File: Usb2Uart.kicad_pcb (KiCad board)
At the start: 2 copper layers, 46.2 x 16.2 mm, 46 parts, among them Q1 DVIUC6-4SC6, U1 DLW21SN900SQ2

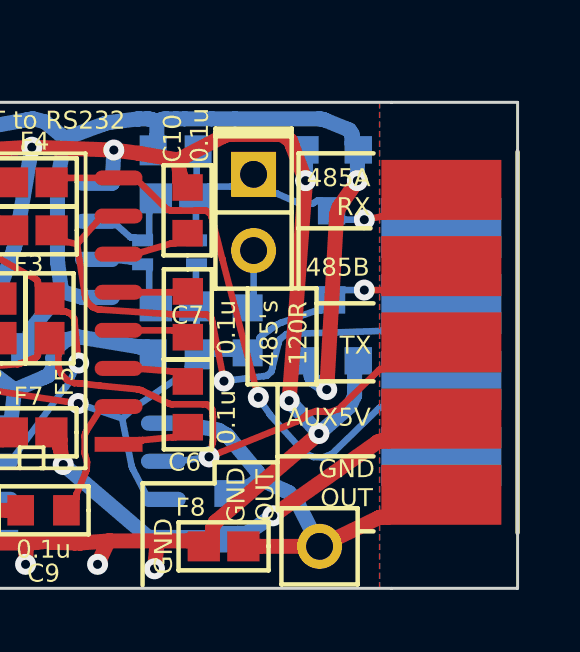
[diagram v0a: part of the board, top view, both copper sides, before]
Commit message: Connector mirrored as it should be
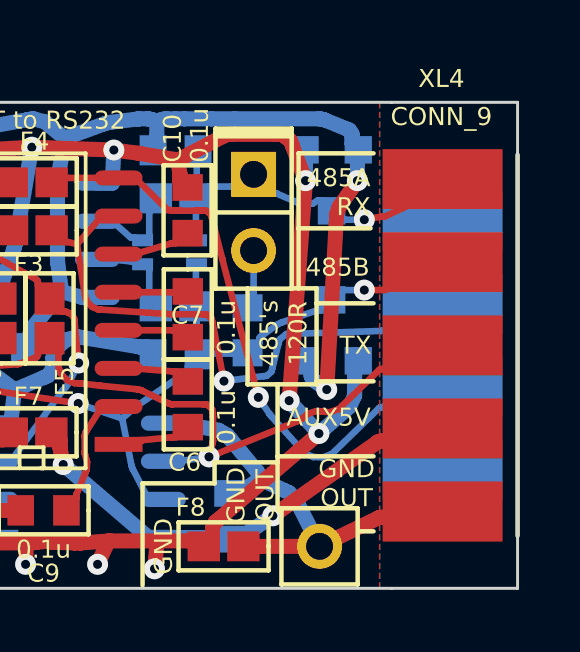
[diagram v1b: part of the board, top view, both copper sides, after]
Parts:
- moved XL4 0.10 mm to (183.2, 88.5)
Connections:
- DD1 pad 10: (no net) -> Net-(DD1-Pad10)
- DD1 pad 12: (no net) -> Net-(DD1-Pad12)
- DD1 pad 19: (no net) -> Net-(DD1-Pad19)
- DD1 pad 2: (no net) -> Net-(DD1-Pad2)
- DD1 pad 24: (no net) -> Net-(DD1-Pad24)
- DD1 pad 27: (no net) -> Net-(DD1-Pad27)
- DD1 pad 28: (no net) -> Net-(DD1-Pad28)
- DD1 pad 6: (no net) -> Net-(DD1-Pad6)
- DD1 pad 8: (no net) -> Net-(DD1-Pad8)
- DD1 pad 9: (no net) -> Net-(DD1-Pad9)
- Q1 pad 3: (no net) -> Net-(Q1-Pad3)
- Q1 pad 4: (no net) -> Net-(Q1-Pad4)
- XL4 pad 6: (no net) -> Net-(XL4-Pad6)
- XL4 pad 9: (no net) -> Net-(XL4-Pad9)

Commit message: toporrrrrr
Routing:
- net /RTS: track 19.6 -> 29.3 mm, vias 1 -> 2
- net /CTS: track 20.0 -> 10.2 mm, vias 1 -> 0
- net /Aux5V: track 15.9 -> 12.1 mm
- net /RS485B_RX: track 30.3 -> 34.1 mm
- removed copper zone on F.Cu, net /SHLD
- removed copper zone on B.Cu, net GND
- removed copper zone on F.Cu, net GND

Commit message: gerber add
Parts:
- moved XL5 13.2 mm to (177.2, 82.0)
- moved D4 10.8 mm to (176.8, 93.8), turned to 0 degrees
- moved D5 1.96 mm to (176.8, 89.9)
- moved F1 0.74 mm to (171.8, 84.3)
- moved R5 0.72 mm to (171.8, 82.7)
- moved U1 0.55 mm to (171.7, 85.9)
- moved C6 0.47 mm to (172.2, 90.9)
- moved F7 0.47 mm to (166.7, 91.8)
- moved F8 0.42 mm to (173.4, 94.8)
- moved F2 0.37 mm to (171.8, 87.6)
- moved R7 0.37 mm to (171.8, 89.2)
- moved C13 0.32 mm to (173.9, 94.3)
- moved F5 0.26 mm to (167.6, 87.3)
- moved F6 0.26 mm to (166.0, 87.3)
- moved C11 0.14 mm to (165.9, 88.6)
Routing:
- net GND: track 159.8 -> 129.8 mm, vias 27 -> 20
- net /RTS: track 29.3 -> 15.7 mm, vias 2 -> 1
- net /RS485A: track 12.5 -> 22.9 mm, vias 1 -> 3
- net /Aux5V: track 12.1 -> 20.7 mm
- net GNDPWR: track 15.1 -> 20.9 mm, vias 0 -> 2
- net /CTS: track 10.2 -> 15.9 mm, vias 0 -> 1
- net /RS485B_RX: track 34.1 -> 30.6 mm
- net +3.3V: track 72.4 -> 74.8 mm, vias 4 -> 2
- net /TXDEN: track 17.6 -> 15.7 mm
- net +5V: track 46.1 -> 44.3 mm
- net /RX_LED: track 12.0 -> 10.3 mm
- net /TX: track 22.5 -> 23.7 mm
- net /UART_TX: track 29.8 -> 29.0 mm
- net /USB_IN_1: track 8.89 -> 8.12 mm
- net /UART_RX: track 18.1 -> 17.6 mm, vias 2 -> 1
- added copper zone on B.Cu, net GND
- added copper zone on F.Cu, net GND
